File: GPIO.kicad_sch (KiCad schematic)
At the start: 14 parts, among them Q10 Q_PNP_BEC, U10 PCF8574T, U9 ATtiny85V-10S

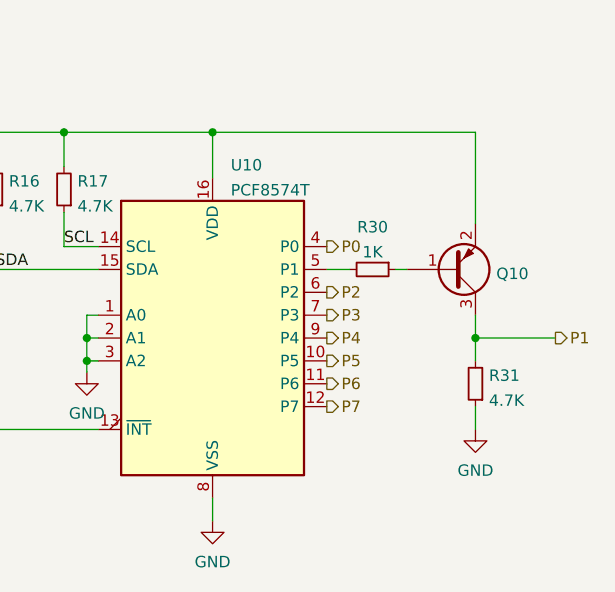
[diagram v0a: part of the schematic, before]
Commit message: A try to add pull-up resistor for gpio_out
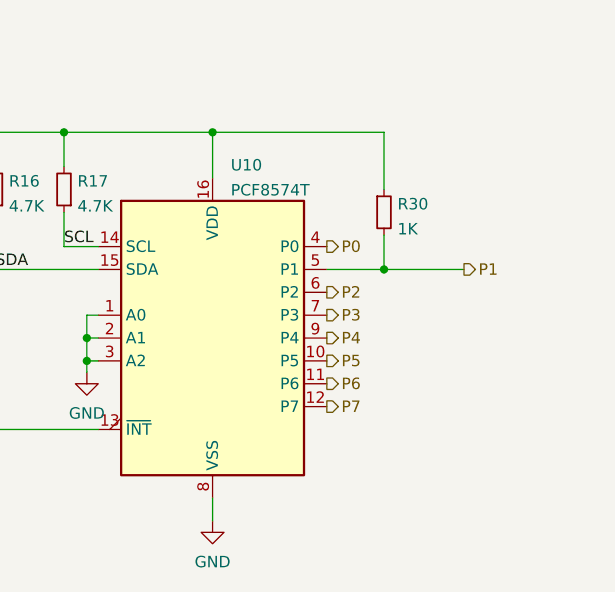
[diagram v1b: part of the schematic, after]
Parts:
- removed Q10: Q_PNP_BEC, Package_TO_SOT_SMD:SOT-23, symbol Device:Q_PNP_BEC
- removed R31: 4.7K, Resistor_SMD:R_0603_1608Metric, symbol Device:R_Small
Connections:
- net 5V: now also R30.1
- net P1: now also R30.2, U10.5 (P1)
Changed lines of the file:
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@@
 (kicad_sch (version 20211123) (generator eeschema)
   (paper "A4")
+  (junction (at 201.93 96.52) (diameter 0) (color 0 0 0 0)
+  )
   (junction (at 182.88 81.28) (diameter 0) (color 0 0 0 0)
   )
@@
   )
   (junction (at 168.91 106.68) (diameter 0) (color 0 0 0 0)
-  )
-  (junction (at 212.09 104.14) (diameter 0) (color 0 0 0 0)
   )
   (junction (at 110.49 81.28) (diameter 0) (color 0 0 0 0)
@@
   (no_connect (at 125.73 97.79))
   (no_connect (at 125.73 107.95))
-  (wire (pts (xy 212.09 104.14) (xy 220.98 104.14))
+  (wire (pts (xy 201.93 96.52) (xy 210.82 96.52))
     (stroke (width 0) (type default) (color 0 0 0 0))
   )
@@
     (stroke (width 0) (type default) (color 0 0 0 0))
   )
-  (wire (pts (xy 195.58 96.52) (xy 198.12 96.52))
-    (stroke (width 0) (type default) (color 0 0 0 0))
-  )
   (wire (pts (xy 125.73 105.41) (xy 128.27 105.41))
     (stroke (width 0) (type default) (color 0 0 0 0))
@@
     (stroke (width 0) (type default) (color 0 0 0 0))
   )
-  (wire (pts (xy 212.09 104.14) (xy 212.09 106.68))
-    (stroke (width 0) (type default) (color 0 0 0 0))
-  )
   (wire (pts (xy 152.4 81.28) (xy 158.75 81.28))
     (stroke (width 0) (type default) (color 0 0 0 0))
   )
-  (wire (pts (xy 212.09 101.6) (xy 212.09 104.14))
+  (wire (pts (xy 201.93 92.71) (xy 201.93 96.52))
     (stroke (width 0) (type default) (color 0 0 0 0))
   )
@@
     (stroke (width 0) (type default) (color 0 0 0 0))
   )
-  (wire (pts (xy 203.2 96.52) (xy 204.47 96.52))
-    (stroke (width 0) (type default) (color 0 0 0 0))
-  )
   (wire (pts (xy 110.49 81.28) (xy 137.16 81.28))
     (stroke (width 0) (type default) (color 0 0 0 0))
@@
     (stroke (width 0) (type default) (color 0 0 0 0))
   )
-  (wire (pts (xy 212.09 111.76) (xy 212.09 114.3))
-    (stroke (width 0) (type default) (color 0 0 0 0))
-  )
-  (wire (pts (xy 182.88 81.28) (xy 212.09 81.28))
+  (wire (pts (xy 182.88 81.28) (xy 201.93 81.28))
     (stroke (width 0) (type default) (color 0 0 0 0))
   )
@@
     (stroke (width 0) (type default) (color 0 0 0 0))
   )
+  (wire (pts (xy 195.58 96.52) (xy 201.93 96.52))
+    (stroke (width 0) (type default) (color 0 0 0 0))
+  )
   (wire (pts (xy 137.16 102.87) (xy 146.05 102.87))
     (stroke (width 0) (type default) (color 0 0 0 0))
@@
     (stroke (width 0) (type default) (color 0 0 0 0))
   )
-  (wire (pts (xy 212.09 81.28) (xy 212.09 91.44))
+  (wire (pts (xy 201.93 81.28) (xy 201.93 87.63))
     (stroke (width 0) (type default) (color 0 0 0 0))
   )
@@
     (effects (font (size 1.27 1.27)) (justify left bottom))
   )
-  (hierarchical_label "P1" (shape output) (at 220.98 104.14 0)
+  (hierarchical_label "P1" (shape output) (at 210.82 96.52 0)
     (effects (font (size 1.27 1.27)) (justify left))
   )
@@
     (pin "9")
   )
-  (symbol (lib_id "Device:R_Small") (at 200.66 96.52 270) (unit 1)
-    (in_bom yes) (on_board yes) (fields_autoplaced)
-    (property "Reference" "R30" (id 0) (at 200.66 91.8169 90))
-    (property "Value" "1K" (id 1) (at 200.66 94.592 90))
-    (property "Footprint" "Resistor_SMD:R_0603_1608Metric" (id 2) (at 200.66 96.52 0)
-      (effects (font (size 1.27 1.27)) hide)
-    )
-    (property "Datasheet" "~" (id 3) (at 200.66 96.52 0)
-      (effects (font (size 1.27 1.27)) hide)
-    )
-    (pin "1")
-    (pin "2")
-  )
   (symbol (lib_id "Device:R_Small") (at 130.81 105.41 90) (unit 1)
     (in_bom yes) (on_board yes)
@@
     )
     (pin "1")
-  )
-  (symbol (lib_id "power:GND") (at 212.09 114.3 0) (unit 1)
-    (in_bom yes) (on_board yes) (fields_autoplaced)
-    (property "Reference" "#PWR0135" (id 0) (at 212.09 120.65 0)
-      (effects (font (size 1.27 1.27)) hide)
-    )
-    (property "Value" "GND" (id 1) (at 212.09 118.8625 0))
-    (property "Footprint" "" (id 2) (at 212.09 114.3 0)
-      (effects (font (size 1.27 1.27)) hide)
-    )
-    (property "Datasheet" "" (id 3) (at 212.09 114.3 0)
-      (effects (font (size 1.27 1.27)) hide)
-    )
-    (pin "1")
-  )
-  (symbol (lib_id "Device:R_Small") (at 212.09 109.22 180) (unit 1)
-    (in_bom yes) (on_board yes) (fields_autoplaced)
-    (property "Reference" "R31" (id 0) (at 213.5886 108.3115 0)
-      (effects (font (size 1.27 1.27)) (justify right))
-    )
-    (property "Value" "4.7K" (id 1) (at 213.5886 111.0866 0)
-      (effects (font (size 1.27 1.27)) (justify right))
-    )
-    (property "Footprint" "Resistor_SMD:R_0603_1608Metric" (id 2) (at 212.09 109.22 0)
-      (effects (font (size 1.27 1.27)) hide)
-    )
-    (property "Datasheet" "~" (id 3) (at 212.09 109.22 0)
-      (effects (font (size 1.27 1.27)) hide)
-    )
-    (pin "1")
-    (pin "2")
   )
   (symbol (lib_id "power:GND") (at 110.49 120.65 0) (unit 1)
@@
     (pin "8")
   )
+  (symbol (lib_id "Device:R_Small") (at 201.93 90.17 0) (unit 1)
+    (in_bom yes) (on_board yes) (fields_autoplaced)
+    (property "Reference" "R30" (id 0) (at 203.4286 89.2615 0)
+      (effects (font (size 1.27 1.27)) (justify left))
+    )
+    (property "Value" "1K" (id 1) (at 203.4286 92.0366 0)
+      (effects (font (size 1.27 1.27)) (justify left))
+    )
+    (property "Footprint" "Resistor_SMD:R_0603_1608Metric" (id 2) (at 201.93 90.17 0)
+      (effects (font (size 1.27 1.27)) hide)
+    )
+    (property "Datasheet" "~" (id 3) (at 201.93 90.17 0)
+      (effects (font (size 1.27 1.27)) hide)
+    )
+    (pin "1")
+    (pin "2")
+  )
   (symbol (lib_id "Device:C_Small") (at 73.66 96.52 0) (unit 1)
     (in_bom yes) (on_board yes) (fields_autoplaced)
@@
     (pin "2")
   )
-  (symbol (lib_id "Device:Q_PNP_BEC") (at 209.55 96.52 0) (mirror x) (unit 1)
-    (in_bom yes) (on_board yes) (fields_autoplaced)
-    (property "Reference" "Q10" (id 0) (at 214.4014 96.999 0)
-      (effects (font (size 1.27 1.27)) (justify left))
-    )
-    (property "Value" "Q_PNP_BEC" (id 1) (at 214.4014 98.3866 0)
-      (effects (font (size 1.27 1.27)) (justify left) hide)
-    )
-    (property "Footprint" "Package_TO_SOT_SMD:SOT-23" (id 2) (at 214.63 99.06 0)
-      (effects (font (size 1.27 1.27)) hide)
-    )
-    (property "Datasheet" "~" (id 3) (at 209.55 96.52 0)
-      (effects (font (size 1.27 1.27)) hide)
-    )
-    (pin "1")
-    (pin "2")
-    (pin "3")
-  )
   (symbol (lib_id "Device:R_Small") (at 158.75 87.63 180) (unit 1)

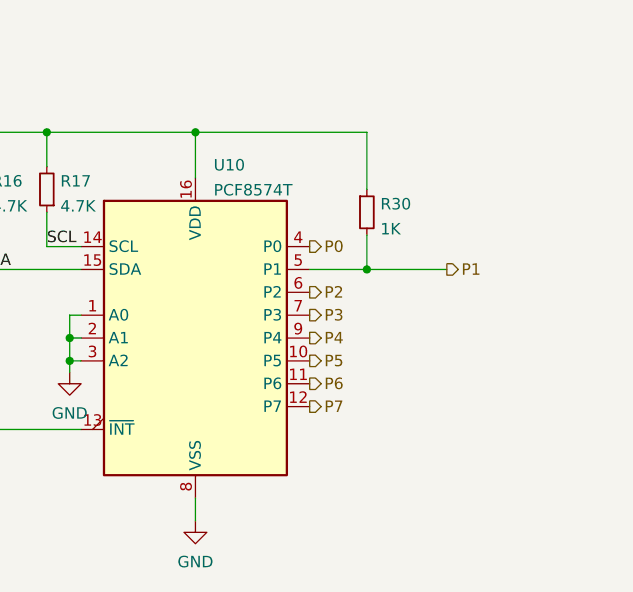
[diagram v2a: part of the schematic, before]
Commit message: Return to PNP-out
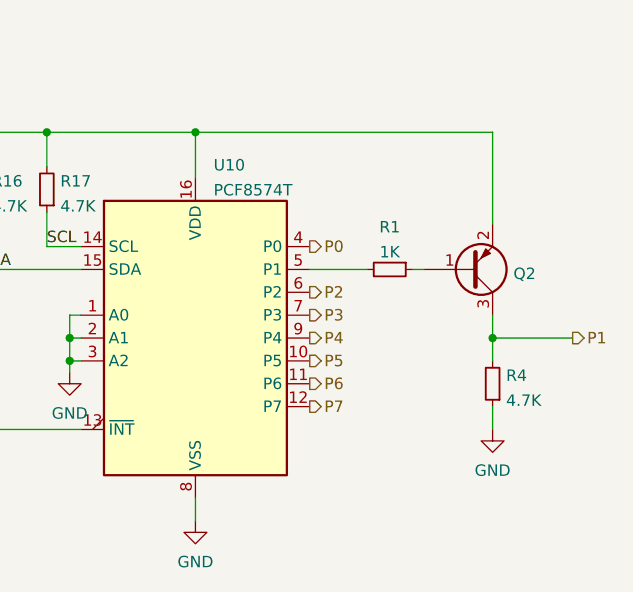
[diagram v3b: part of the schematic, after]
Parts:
- removed R30: 1K, Resistor_SMD:R_0603_1608Metric, symbol Device:R_Small
- added Q2: Q_PNP_BEC, Package_TO_SOT_SMD:SOT-23, symbol Device:Q_PNP_BEC
- added R1: 1K, Resistor_SMD:R_0603_1608Metric, symbol Device:R_Small
- added R4: 4.7K, Resistor_SMD:R_0603_1608Metric, symbol Device:R_Small
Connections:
- net 5V: now also Q2.2 (E)
- net GND: now also R4.1
- net P1: now also Q2.3 (C), R4.2; no longer U10.5 (P1)
- new net: Q2.1 (B), R1.1
- new net: R1.2, U10.5 (P1)
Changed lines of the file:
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@@
 (kicad_sch (version 20230121) (generator eeschema)
   (paper "A4")
-  (junction (at 201.93 96.52) (diameter 0) (color 0 0 0 0)
-  )
   (junction (at 182.88 81.28) (diameter 0) (color 0 0 0 0)
   )
@@
   )
   (junction (at 152.4 81.28) (diameter 0) (color 0 0 0 0)
+  )
+  (junction (at 215.9 104.14) (diameter 0) (color 0 0 0 0)
   )
   (junction (at 166.37 81.28) (diameter 0) (color 0 0 0 0)
@@
   (no_connect (at 125.73 97.79))
   (no_connect (at 125.73 107.95))
-  (wire (pts (xy 201.93 96.52) (xy 210.82 96.52))
-    (stroke (width 0) (type default))
-  )
   (wire (pts (xy 133.35 105.41) (xy 146.05 105.41))
     (stroke (width 0) (type default))
   )
+  (wire (pts (xy 215.9 111.76) (xy 215.9 114.3))
+    (stroke (width 0) (type default))
+  )
+  (wire (pts (xy 215.9 81.28) (xy 215.9 91.44))
+    (stroke (width 0) (type default))
+  )
   (wire (pts (xy 182.88 81.28) (xy 182.88 86.36))
     (stroke (width 0) (type default))
@@
     (stroke (width 0) (type default))
   )
-  (wire (pts (xy 201.93 92.71) (xy 201.93 96.52))
-    (stroke (width 0) (type default))
-  )
   (wire (pts (xy 158.75 81.28) (xy 158.75 85.09))
     (stroke (width 0) (type default))
@@
     (stroke (width 0) (type default))
   )
+  (wire (pts (xy 215.9 104.14) (xy 224.79 104.14))
+    (stroke (width 0) (type default))
+  )
   (wire (pts (xy 110.49 81.28) (xy 137.16 81.28))
     (stroke (width 0) (type default))
@@
     (stroke (width 0) (type default))
   )
+  (wire (pts (xy 215.9 104.14) (xy 215.9 106.68))
+    (stroke (width 0) (type default))
+  )
   (wire (pts (xy 137.16 97.79) (xy 137.16 102.87))
     (stroke (width 0) (type default))
@@
     (stroke (width 0) (type default))
   )
-  (wire (pts (xy 182.88 81.28) (xy 201.93 81.28))
+  (wire (pts (xy 182.88 81.28) (xy 215.9 81.28))
     (stroke (width 0) (type default))
   )
@@
     (stroke (width 0) (type default))
   )
-  (wire (pts (xy 201.93 81.28) (xy 201.93 87.63))
+  (wire (pts (xy 215.9 101.6) (xy 215.9 104.14))
+    (stroke (width 0) (type default))
+  )
+  (wire (pts (xy 207.01 96.52) (xy 208.28 96.52))
     (stroke (width 0) (type default))
   )
@@
     (effects (font (size 1.27 1.27)) (justify left bottom))
   )
-  (hierarchical_label "P1" (shape output) (at 210.82 96.52 0) (fields_autoplaced)
-    (effects (font (size 1.27 1.27)) (justify left))
-  )
   (hierarchical_label "D+" (shape bidirectional) (at 146.05 105.41 0) (fields_autoplaced)
     (effects (font (size 1.27 1.27)) (justify left))
@@
   )
   (hierarchical_label "P6" (shape output) (at 195.58 109.22 0) (fields_autoplaced)
+    (effects (font (size 1.27 1.27)) (justify left))
+  )
+  (hierarchical_label "P1" (shape output) (at 224.79 104.14 0) (fields_autoplaced)
     (effects (font (size 1.27 1.27)) (justify left))
   )
@@
   (hierarchical_label "5V" (shape input) (at 62.23 91.44 180) (fields_autoplaced)
     (effects (font (size 1.27 1.27)) (justify right))
+  )
+  (symbol (lib_id "Device:Q_PNP_BEC") (at 213.36 96.52 0) (mirror x) (unit 1)
+    (in_bom yes) (on_board yes) (dnp no) (fields_autoplaced)
+    (property "Reference" "Q2" (at 218.2114 96.999 0)
+      (effects (font (size 1.27 1.27)) (justify left))
+    )
+    (property "Value" "Q_PNP_BEC" (at 218.2114 98.3866 0)
+      (effects (font (size 1.27 1.27)) (justify left) hide)
+    )
+    (property "Footprint" "Package_TO_SOT_SMD:SOT-23" (at 218.44 99.06 0)
+      (effects (font (size 1.27 1.27)) hide)
+    )
+    (property "Datasheet" "~" (at 213.36 96.52 0)
+      (effects (font (size 1.27 1.27)) hide)
+    )
+    (pin "1")
+    (pin "2")
+    (pin "3")
+    (instances
+      (project "USB2GPIO"
+        (path "/affe2a42-bf9f-428c-8852-69dcfd2559da/570d9097-1128-4fa1-99b5-d86d067d304c"
+          (reference "Q2") (unit 1)
+        )
+      )
+    )
   )
   (symbol (lib_id "Device:R_Small") (at 152.4 87.63 180) (unit 1)
@@
         (path "/affe2a42-bf9f-428c-8852-69dcfd2559da/570d9097-1128-4fa1-99b5-d86d067d304c"
           (reference "#PWR0133") (unit 1)
+        )
+      )
+    )
+  )
+  (symbol (lib_id "power:GND") (at 215.9 114.3 0) (unit 1)
+    (in_bom yes) (on_board yes) (dnp no) (fields_autoplaced)
+    (property "Reference" "#PWR03" (at 215.9 120.65 0)
+      (effects (font (size 1.27 1.27)) hide)
+    )
+    (property "Value" "GND" (at 215.9 118.8625 0)
+      (effects (font (size 1.27 1.27)))
+    )
+    (property "Footprint" "" (at 215.9 114.3 0)
+      (effects (font (size 1.27 1.27)) hide)
+    )
+    (property "Datasheet" "" (at 215.9 114.3 0)
+      (effects (font (size 1.27 1.27)) hide)
+    )
+    (pin "1")
+    (instances
+      (project "USB2GPIO"
+        (path "/affe2a42-bf9f-428c-8852-69dcfd2559da/570d9097-1128-4fa1-99b5-d86d067d304c"
+          (reference "#PWR03") (unit 1)
         )
       )
@@
     )
   )
+  (symbol (lib_id "Device:R_Small") (at 215.9 109.22 180) (unit 1)
+    (in_bom yes) (on_board yes) (dnp no) (fields_autoplaced)
+    (property "Reference" "R4" (at 217.3986 108.3115 0)
+      (effects (font (size 1.27 1.27)) (justify right))
+    )
+    (property "Value" "4.7K" (at 217.3986 111.0866 0)
+      (effects (font (size 1.27 1.27)) (justify right))
+    )
+    (property "Footprint" "Resistor_SMD:R_0603_1608Metric" (at 215.9 109.22 0)
+      (effects (font (size 1.27 1.27)) hide)
+    )
+    (property "Datasheet" "~" (at 215.9 109.22 0)
+      (effects (font (size 1.27 1.27)) hide)
+    )
+    (pin "1")
+    (pin "2")
+    (instances
+      (project "USB2GPIO"
+        (path "/affe2a42-bf9f-428c-8852-69dcfd2559da/570d9097-1128-4fa1-99b5-d86d067d304c"
+          (reference "R4") (unit 1)
+        )
+      )
+    )
+  )
   (symbol (lib_id "Device:R_Small") (at 130.81 105.41 90) (unit 1)
     (in_bom yes) (on_board yes) (dnp no)
@@
     )
   )
-  (symbol (lib_id "Device:R_Small") (at 201.93 90.17 0) (unit 1)
-    (in_bom yes) (on_board yes) (dnp no) (fields_autoplaced)
-    (property "Reference" "R30" (at 203.4286 89.2615 0)
-      (effects (font (size 1.27 1.27)) (justify left))
-    )
-    (property "Value" "1K" (at 203.4286 92.0366 0)
-      (effects (font (size 1.27 1.27)) (justify left))
-    )
-    (property "Footprint" "Resistor_SMD:R_0603_1608Metric" (at 201.93 90.17 0)
-      (effects (font (size 1.27 1.27)) hide)
-    )
-    (property "Datasheet" "~" (at 201.93 90.17 0)
-      (effects (font (size 1.27 1.27)) hide)
-    )
-    (pin "1")
-    (pin "2")
-    (instances
-      (project "USB2GPIO"
-        (path "/affe2a42-bf9f-428c-8852-69dcfd2559da/570d9097-1128-4fa1-99b5-d86d067d304c"
-          (reference "R30") (unit 1)
-        )
-      )
+  (symbol (lib_id "Device:R_Small") (at 204.47 96.52 270) (unit 1)
+    (in_bom yes) (on_board yes) (dnp no) (fields_autoplaced)
+    (property "Reference" "R1" (at 204.47 91.8169 90)
+      (effects (font (size 1.27 1.27)))
+    )
+    (property "Value" "1K" (at 204.47 94.592 90)
+      (effects (font (size 1.27 1.27)))
+    )
+    (property "Footprint" "Resistor_SMD:R_0603_1608Metric" (at 204.47 96.52 0)
+      (effects (font (size 1.27 1.27)) hide)
+    )
+    (property "Datasheet" "~" (at 204.47 96.52 0)
+      (effects (font (size 1.27 1.27)) hide)
+    )
+    (pin "1")
+    (pin "2")
+    (instances
+      (project "USB2GPIO"
+        (path "/affe2a42-bf9f-428c-8852-69dcfd2559da/570d9097-1128-4fa1-99b5-d86d067d304c"
+          (reference "R1") (unit 1)
+        )
+      )
